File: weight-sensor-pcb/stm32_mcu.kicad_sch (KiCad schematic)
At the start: 2 parts, among them J1 JTAG Connector, U4 STM32F042F4P6

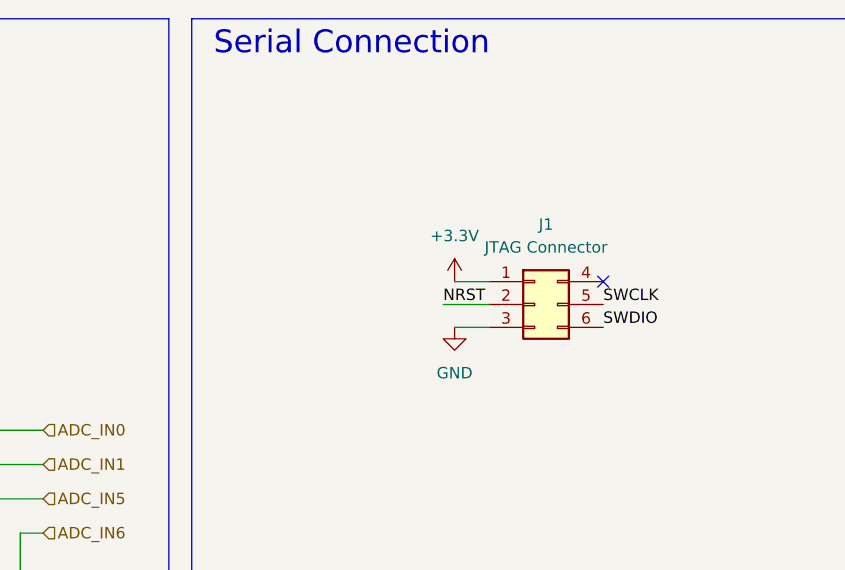
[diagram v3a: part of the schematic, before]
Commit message: updated tag-connect SWD schematic symbol
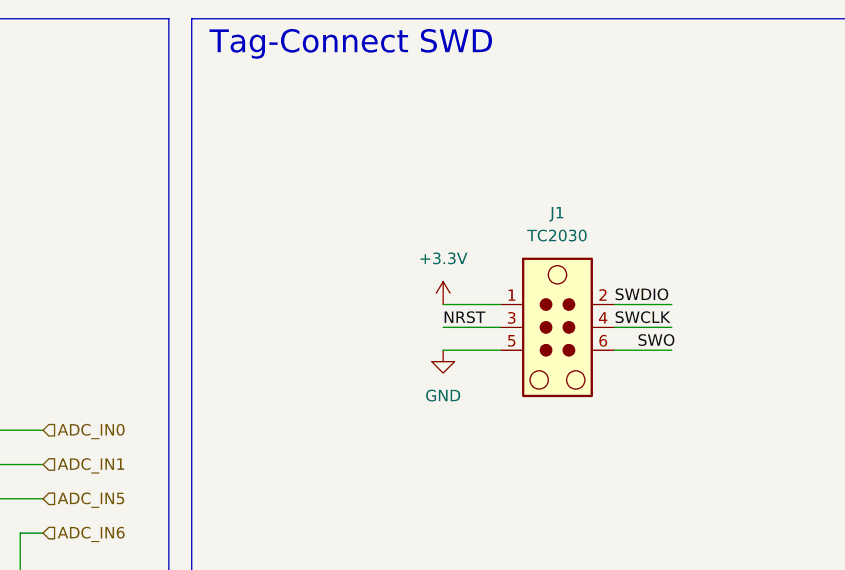
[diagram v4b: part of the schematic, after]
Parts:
- removed J1: JTAG Connector, Capstone:TC2030-IDC-NL, symbol Connector_Generic:Conn_02x03_Top_Bottom
- added J1: TC2030, Connector:Tag-Connect_TC2030-IDC-NL_2x03_P1.27mm_Vertical, symbol Connector:TC2030
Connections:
- net +3.3V: now also J1.1
- net GND: now also J1.5
- net NRST: now also J1.3
- net SWCLK: now also J1.4
- net SWDIO: now also J1.2
- new net SWO: J1.6
- no-connect marks 3 -> 2
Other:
- note added: "Tag-Connect SWD"
- note removed: "Serial Connection"
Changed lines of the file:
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@@
 		)
 	)
-	(text "Serial Connection"
+	(text "Tag-Connect SWD\n"
 		(exclude_from_sim no)
 		(at 219.71 16.764 0)
@@
 	)
 	(no_connect
-		(at 247.65 43.18)
-	)
-	(no_connect
 		(at 130.81 77.47)
 	)
@@
 	(wire
 		(pts
-			(xy 231.14 48.26) (xy 234.95 48.26)
-		)
-		(stroke
-			(width 0)
-			(type default)
-		)
-	)
-	(wire
-		(pts
 			(xy 182.88 87.63) (xy 166.37 87.63)
 		)
@@
 	(wire
 		(pts
+			(xy 236.22 45.72) (xy 229.87 45.72)
+		)
+		(stroke
+			(width 0)
+			(type default)
+		)
+	)
+	(wire
+		(pts
 			(xy 182.88 71.12) (xy 182.88 87.63)
 		)
@@
 	(wire
 		(pts
+			(xy 248.92 50.8) (xy 255.27 50.8)
+		)
+		(stroke
+			(width 0)
+			(type default)
+		)
+	)
+	(wire
+		(pts
 			(xy 116.84 85.09) (xy 130.81 85.09)
 		)
@@
 	(wire
 		(pts
+			(xy 248.92 45.72) (xy 255.27 45.72)
+		)
+		(stroke
+			(width 0)
+			(type default)
+		)
+	)
+	(wire
+		(pts
+			(xy 248.92 48.26) (xy 255.27 48.26)
+		)
+		(stroke
+			(width 0)
+			(type default)
+		)
+	)
+	(wire
+		(pts
 			(xy 177.8 63.5) (xy 177.8 74.93)
 		)
@@
 	(wire
 		(pts
-			(xy 229.87 45.72) (xy 234.95 45.72)
-		)
-		(stroke
-			(width 0)
-			(type default)
-		)
-	)
-	(wire
-		(pts
-			(xy 231.14 43.18) (xy 234.95 43.18)
+			(xy 229.87 50.8) (xy 236.22 50.8)
 		)
 		(stroke
@@
 	(wire
 		(pts
+			(xy 229.87 48.26) (xy 236.22 48.26)
+		)
+		(stroke
+			(width 0)
+			(type default)
+		)
+	)
+	(wire
+		(pts
 			(xy 125.73 72.39) (xy 130.81 72.39)
 		)
@@
 		)
 	)
-	(label "SWDIO"
-		(at 247.65 48.26 0)
+	(label "SWCLK"
+		(at 248.92 48.26 0)
 		(effects
 			(font
@@
 		)
 	)
-	(label "NRST"
-		(at 229.87 45.72 0)
-		(effects
-			(font
-				(size 1.27 1.27)
-			)
-			(justify left bottom)
-		)
-	)
 	(label "BOOT_SEL"
 		(at 120.65 87.63 0)
@@
 		)
 	)
+	(label "NRST"
+		(at 229.87 48.26 0)
+		(effects
+			(font
+				(size 1.27 1.27)
+			)
+			(justify left bottom)
+		)
+	)
 	(label "GPIO13"
 		(at 166.37 90.17 0)
@@
 		)
 	)
-	(label "SWCLK"
-		(at 247.65 45.72 0)
-		(effects
-			(font
-				(size 1.27 1.27)
-			)
-			(justify left bottom)
-		)
-	)
 	(label "NRST"
 		(at 125.73 72.39 0)
@@
 		)
 	)
+	(label "SWO"
+		(at 251.46 50.8 0)
+		(effects
+			(font
+				(size 1.27 1.27)
+			)
+			(justify left bottom)
+		)
+	)
 	(label "SWDIO"
 		(at 166.37 97.79 0)
+		(effects
+			(font
+				(size 1.27 1.27)
+			)
+			(justify left bottom)
+		)
+	)
+	(label "SWDIO"
+		(at 248.92 45.72 0)
 		(effects
 			(font
@@
 	)
 	(symbol
-		(lib_id "power:+3.3V")
-		(at 231.14 43.18 0)
+		(lib_id "Connector:TC2030")
+		(at 241.3 48.26 0)
 		(unit 1)
 		(exclude_from_sim no)
-		(in_bom yes)
+		(in_bom no)
 		(on_board yes)
 		(dnp no)
 		(fields_autoplaced yes)
-		(property "Reference" "#PWR014"
-			(at 231.14 46.99 0)
-			(effects
-				(font
-					(size 1.27 1.27)
-				)
-				(hide yes)
-			)
-		)
-		(property "Value" "+3.3V"
-			(at 231.14 38.1 0)
-			(effects
-				(font
-					(size 1.27 1.27)
-				)
-			)
-		)
-		(property "Footprint" ""
-			(at 231.14 43.18 0)
-			(effects
-				(font
-					(size 1.27 1.27)
-				)
-				(hide yes)
-			)
-		)
-		(property "Datasheet" ""
-			(at 231.14 43.18 0)
-			(effects
-				(font
-					(size 1.27 1.27)
-				)
-				(hide yes)
-			)
-		)
-		(property "Description" "Power symbol creates a global label with name \"+3.3V\""
-			(at 231.14 43.18 0)
-			(effects
-				(font
-					(size 1.27 1.27)
-				)
-				(hide yes)
-			)
+		(property "Reference" "J1"
+			(at 242.57 35.56 0)
+			(effects
+				(font
+					(size 1.27 1.27)
+				)
+			)
+		)
+		(property "Value" "TC2030"
+			(at 242.57 38.1 0)
+			(effects
+				(font
+					(size 1.27 1.27)
+				)
+			)
+		)
+		(property "Footprint" "Connector:Tag-Connect_TC2030-IDC-NL_2x03_P1.27mm_Vertical"
+			(at 242.57 48.26 0)
+			(effects
+				(font
+					(size 1.27 1.27)
+				)
+				(hide yes)
+			)
+		)
+		(property "Datasheet" "https://www.tag-connect.com/wp-content/uploads/bsk-pdf-manager/2019/12/TC2030-IDC-NL-Datasheet-Rev-B.pdf"
+			(at 242.57 48.26 0)
+			(effects
+				(font
+					(size 1.27 1.27)
+				)
+				(hide yes)
+			)
+		)
+		(property "Description" "Tag-Connect’s 6-pins connector"
+			(at 241.3 48.26 0)
+			(effects
+				(font
+					(size 1.27 1.27)
+				)
+				(hide yes)
+			)
+		)
+		(pin "3"
+		)
+		(pin "2"
+		)
+		(pin "6"
 		)
 		(pin "1"
+		)
+		(pin "5"
+		)
+		(pin "4"
 		)
 		(instances
 			(project ""
 				(path "/030ca1f5-68f0-4323-9a91-656d7965b13e/d023421c-1516-46ef-aa61-fab015035186"
-					(reference "#PWR014")
+					(reference "J1")
 					(unit 1)
 				)
@@
 	)
 	(symbol
-		(lib_id "Connector_Generic:Conn_02x03_Top_Bottom")
-		(at 240.03 45.72 0)
+		(lib_id "power:+3.3V")
+		(at 229.87 45.72 0)
 		(unit 1)
 		(exclude_from_sim no)
@@
 		(dnp no)
 		(fields_autoplaced yes)
-		(property "Reference" "J1"
-			(at 241.3 36.83 0)
-			(effects
-				(font
-					(size 1.27 1.27)
-				)
-			)
-		)
-		(property "Value" "JTAG Connector"
-			(at 241.3 39.37 0)
-			(effects
-				(font
-					(size 1.27 1.27)
-				)
-			)
-		)
-		(property "Footprint" "Capstone:TC2030-IDC-NL"
-			(at 240.03 45.72 0)
-			(effects
-				(font
-					(size 1.27 1.27)
-				)
-				(hide yes)
-			)
-		)
-		(property "Datasheet" "~"
-			(at 240.03 45.72 0)
-			(effects
-				(font
-					(size 1.27 1.27)
-				)
-				(hide yes)
-			)
-		)
-		(property "Description" "Generic connector, double row, 02x03, top/bottom pin numbering scheme (row 1: 1...pins_per_row, row2: pins_per_row+1 ... num_pins), script generated (kicad-library-utils/schlib/autogen/connector/)"
-			(at 240.03 45.72 0)
-			(effects
-				(font
-					(size 1.27 1.27)
-				)
-				(hide yes)
-			)
-		)
-		(pin "3"
-		)
-		(pin "4"
-		)
-		(pin "6"
-		)
-		(pin "2"
+		(property "Reference" "#PWR017"
+			(at 229.87 49.53 0)
+			(effects
+				(font
+					(size 1.27 1.27)
+				)
+				(hide yes)
+			)
+		)
+		(property "Value" "+3.3V"
+			(at 229.87 40.64 0)
+			(effects
+				(font
+					(size 1.27 1.27)
+				)
+			)
+		)
+		(property "Footprint" ""
+			(at 229.87 45.72 0)
+			(effects
+				(font
+					(size 1.27 1.27)
+				)
+				(hide yes)
+			)
+		)
+		(property "Datasheet" ""
+			(at 229.87 45.72 0)
+			(effects
+				(font
+					(size 1.27 1.27)
+				)
+				(hide yes)
+			)
+		)
+		(property "Description" "Power symbol creates a global label with name \"+3.3V\""
+			(at 229.87 45.72 0)
+			(effects
+				(font
+					(size 1.27 1.27)
+				)
+				(hide yes)
+			)
 		)
 		(pin "1"
 		)
-		(pin "5"
-		)
 		(instances
-			(project ""
+			(project "weight-sensor-pcb"
 				(path "/030ca1f5-68f0-4323-9a91-656d7965b13e/d023421c-1516-46ef-aa61-fab015035186"
-					(reference "J1")
+					(reference "#PWR017")
 					(unit 1)
 				)
@@
 	(symbol
 		(lib_id "power:GND")
-		(at 231.14 48.26 0)
+		(at 229.87 50.8 0)
 		(unit 1)
 		(exclude_from_sim no)
@@
 		(dnp no)
 		(fields_autoplaced yes)
-		(property "Reference" "#PWR013"
-			(at 231.14 54.61 0)
+		(property "Reference" "#PWR018"
+			(at 229.87 57.15 0)
 			(effects
 				(font
@@
 		)
 		(property "Value" "GND"
-			(at 231.14 53.34 0)
+			(at 229.87 55.88 0)
 			(effects
 				(font
@@
 		)
 		(property "Footprint" ""
-			(at 231.14 48.26 0)
+			(at 229.87 50.8 0)
 			(effects
 				(font
@@
 		)
 		(property "Datasheet" ""
-			(at 231.14 48.26 0)
+			(at 229.87 50.8 0)
 			(effects
 				(font
@@
 		)
 		(property "Description" "Power symbol creates a global label with name \"GND\" , ground"
-			(at 231.14 48.26 0)
+			(at 229.87 50.8 0)
 			(effects
 				(font
@@
 		)
 		(instances
-			(project ""
+			(project "weight-sensor-pcb"
 				(path "/030ca1f5-68f0-4323-9a91-656d7965b13e/d023421c-1516-46ef-aa61-fab015035186"
-					(reference "#PWR013")
+					(reference "#PWR018")
 					(unit 1)
 				)

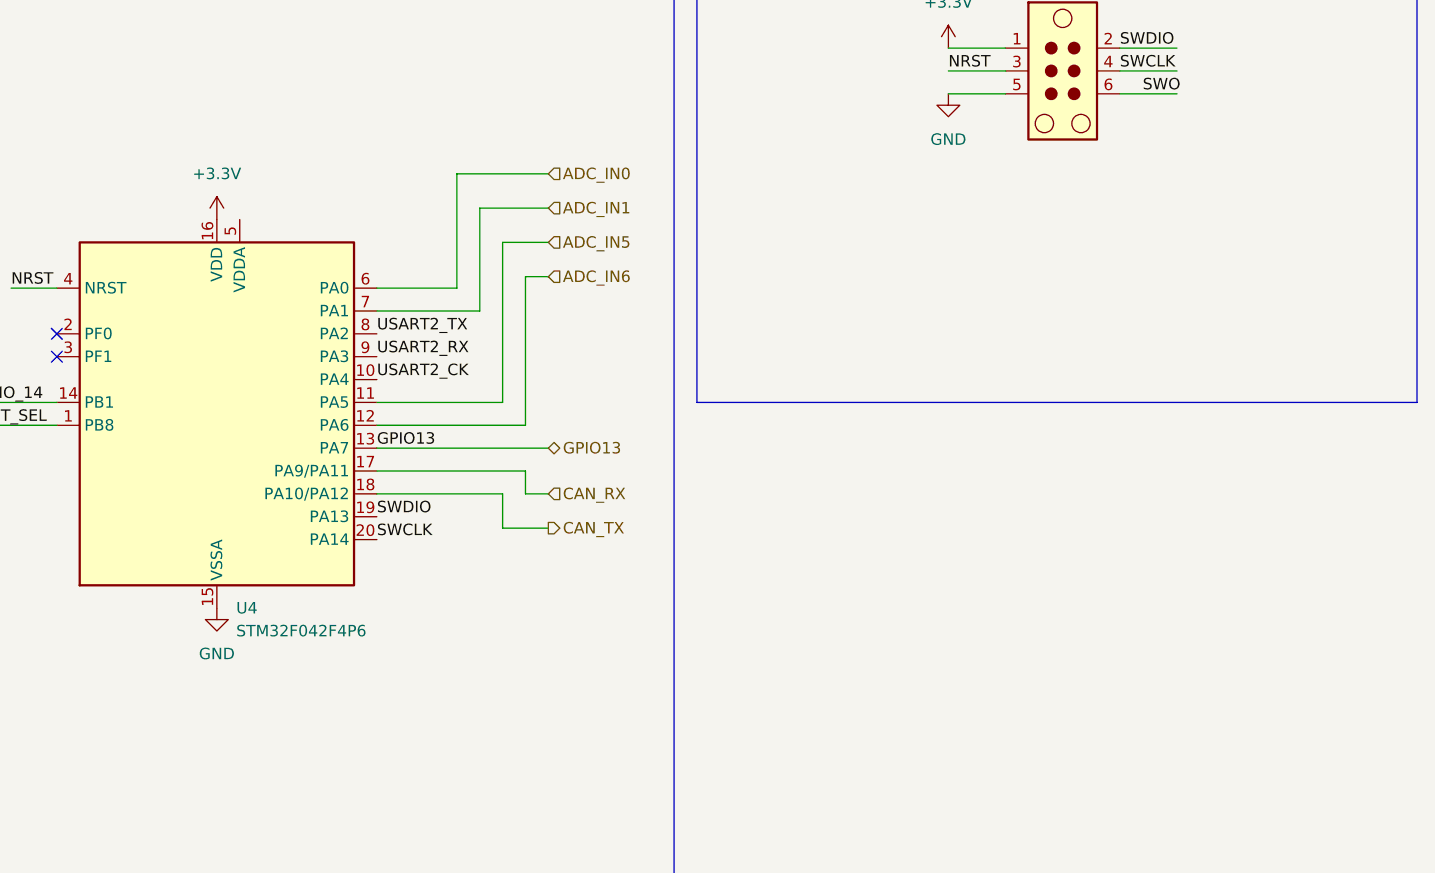
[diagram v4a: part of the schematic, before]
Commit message: Add decoupling capacitors, current limiting resistors for MCU and CAN Transceiver
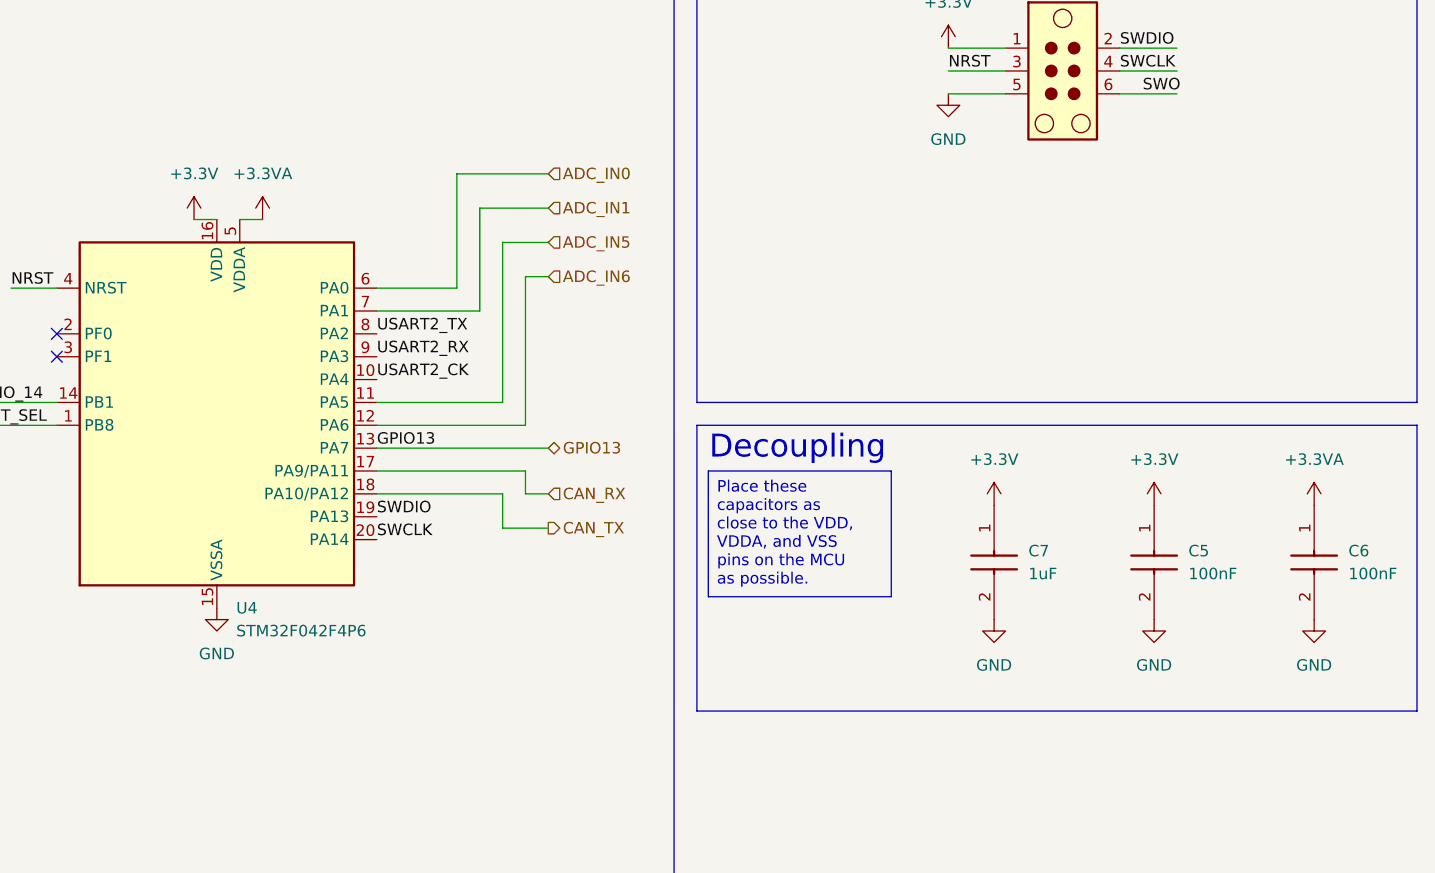
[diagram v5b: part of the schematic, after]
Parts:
- added C5, C6: 100nF, CAPC1005X70N, symbol Capstone:GRM155R70J104KA01D
- added C7: 1uF, CAPC1005X70N, symbol Capstone:GRM155R70J105KA12D
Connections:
- net +3.3V: now also C5.1, C7.1
- net GND: now also C5.2, C6.2, C7.2
- net +3.3VA: now reaches U4.5 (VDDA)
- net +3.3VA: now also C6.1
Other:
- note added: "Decoupling"

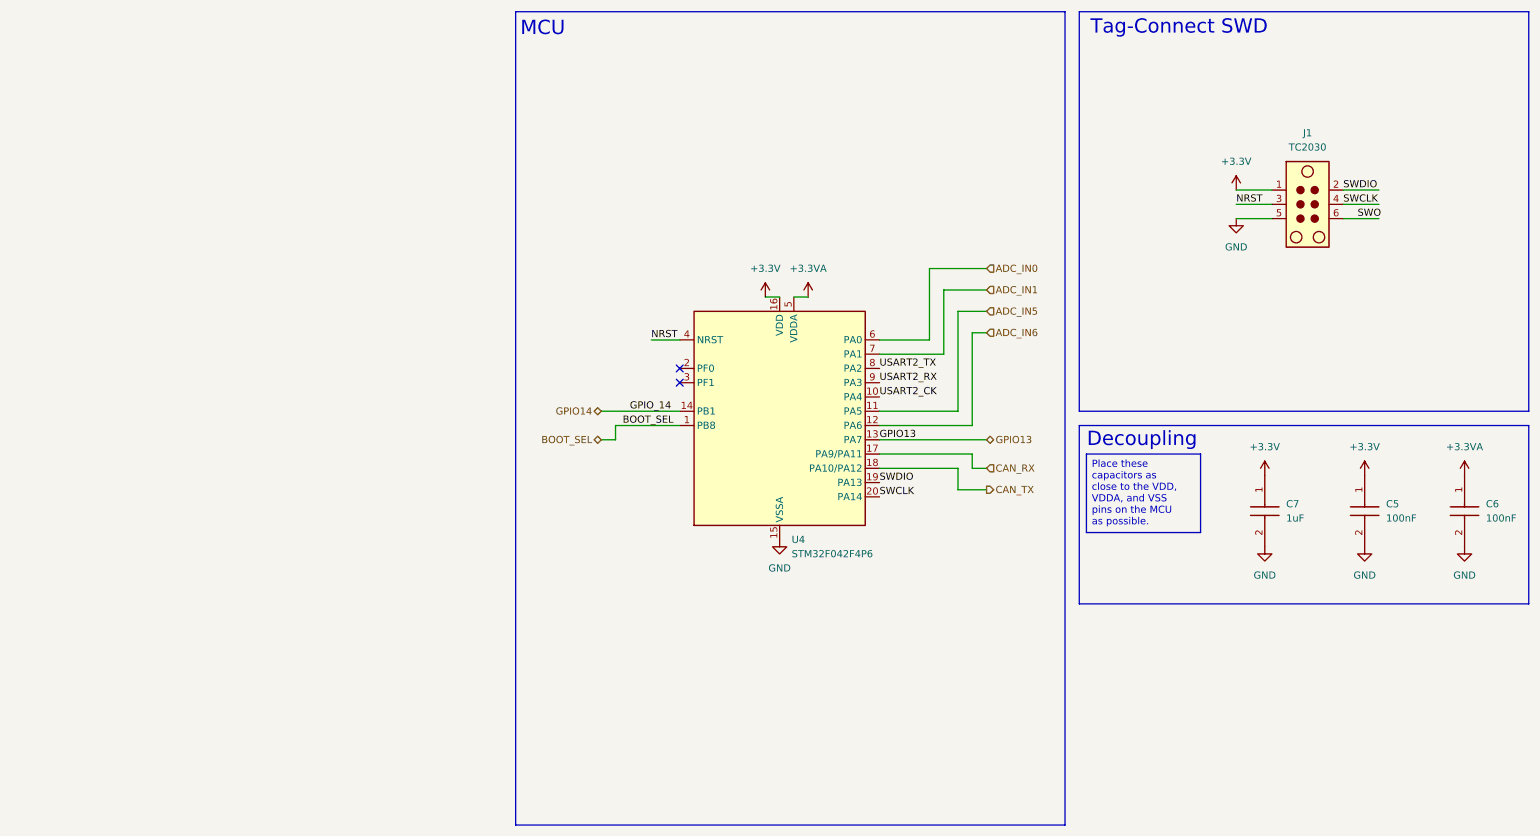
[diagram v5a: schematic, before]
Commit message: Add ferrite bead between VDDA and VDD, add more notes for MCU
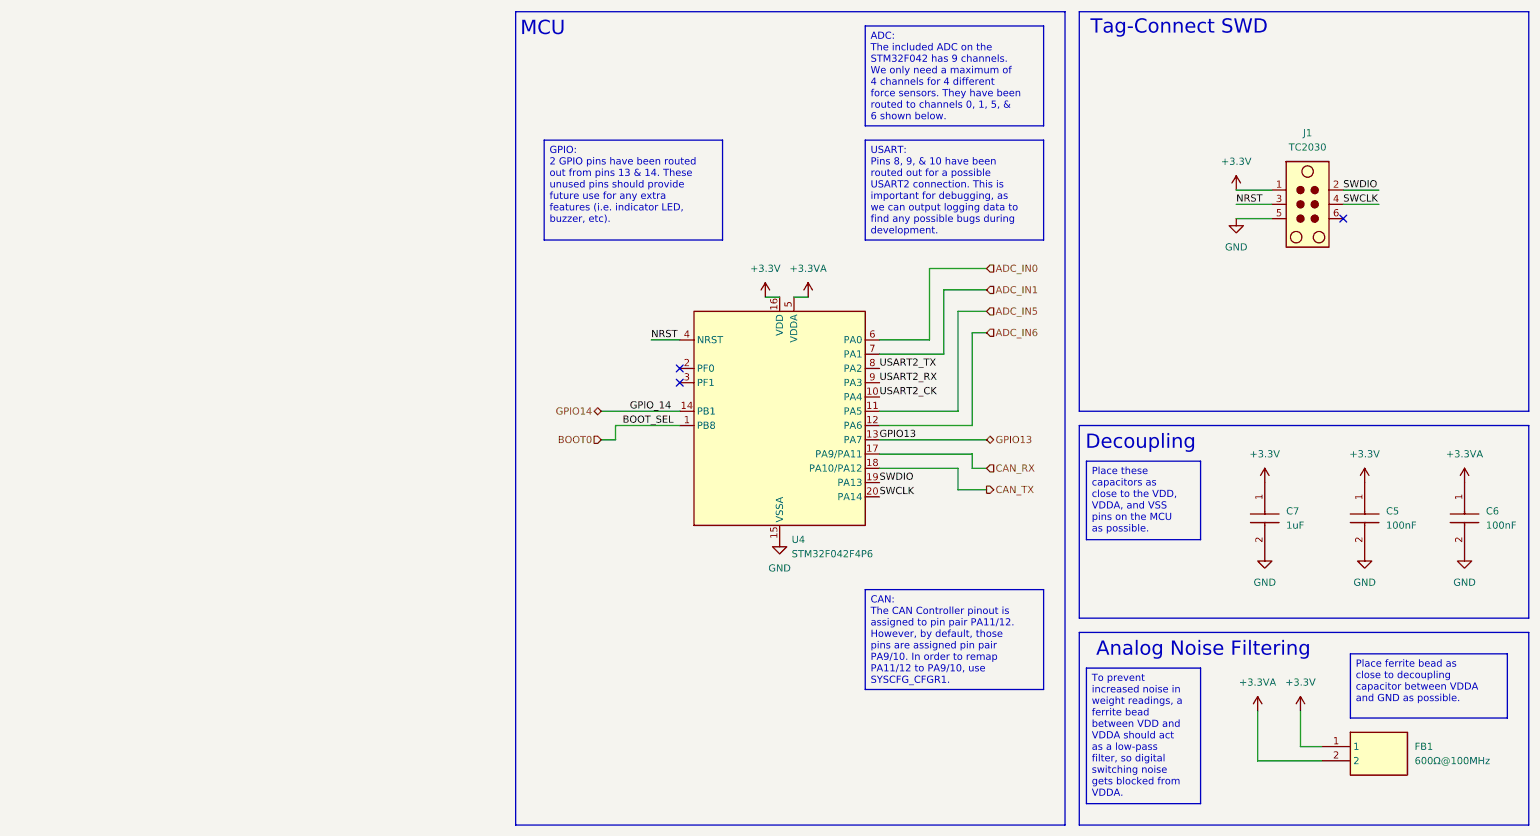
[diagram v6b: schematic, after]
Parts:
- added FB1: 600Ω@100MHz, NFZ15SG152SN10B, symbol Capstone:BLM15AG601SN1D
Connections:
- net +3.3V: now also FB1.1
- net +3.3VA: now also FB1.2
- net BOOT_SEL renamed BOOT0
- net SWO: no longer names the net of J1.6
- no-connect marks 2 -> 3
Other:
- note added: "Analog Noise Filtering"
- moved on the sheet: C5, C6, C7
